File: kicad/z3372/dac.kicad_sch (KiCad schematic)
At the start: 30 parts, among them U13 LM4040AIM3-2.5, U4 TL074, U9 AD5328

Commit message: checkpoint z3372 v0.4
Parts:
- added C27: 10n, Capacitor_SMD:C_0603_1608Metric, symbol Device:C
- added R34: 15k, Resistor_SMD:R_0603_1608Metric, symbol Device:R
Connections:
- net GND: now also C27.2
- net MOD_AMOUNT_VCA3_DAC: no longer U9.13 (VOUT_H)
- net FINAL_VCA4_DAC: now reaches U9.12 (VOUT_G)
- net FINAL_VCA4_DAC: now also R34.1
- new net FINAL_VCA4_CV: C27.1, R34.2
- new net MOD_AMOUNT_DAC: U9.13 (VOUT_H)
- no-connect marks 1 -> 0
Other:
- note added: "AD5328: "B" version works fine. For use at 2X gain output. DAC: 2.5V Reference Voltage B, C, D grades of LM4040 are likely good 'nuff"
- note added: "Pan CVA CV: Take 0V : 5V from DAC shift to -2.5V : 2.5V output 10n cap to give a ~1.6kHz low pass filter TODO: swap inputs and modify filter cap"
- note removed: "AD5328: "B" version works fine. DAC: 2.5V Reference Voltage B, C, D grades of LM4040 are likely good 'nuff"
- note removed: "Pan CVA CV: Take 0V : 5V from DAC shift to -2.5V : 2.5V output 10n cap to give a ~1.6kHz low pass filter"
- title: Z3372 Signal Processing -> Z3372 Signal Processor
- moved on the sheet: C10, C26, C41, C42, C43, C44, C9, R10, R11, R16, R29, R5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

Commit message: schematic done.  some values need tweaking.  design review still needed
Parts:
- removed C10, C27, C44: 10n, Capacitor_SMD:C_0603_1608Metric, symbol Device:C
- removed C39, C7, C8: 0.1u, Capacitor_SMD:C_0603_1608Metric, symbol Device:C
- removed R10, R12, R6, R8: 20k, Resistor_SMD:R_0603_1608Metric, symbol Device:R
- removed R34, R77: 15k, Resistor_SMD:R_0603_1608Metric, symbol Device:R
- removed R47: 4k7, Resistor_SMD:R_1206_3216Metric, symbol Device:R
- removed U13: LM4040AIM3-2.5, Package_TO_SOT_SMD:SOT-23, symbol Reference_Voltage:LM4040DBZ-2.5
- removed U4: TL074, Package_SO:SOIC-14_3.9x8.7mm_P1.27mm, symbol Amplifier_Operational:TL074
- added U3: TL074, Package_SO:SOIC-14_3.9x8.7mm_P1.27mm, symbol Amplifier_Operational:TL074
- C26: value 22n -> 68n; LCSC Part C21122 -> C31658
- U9: symbol as3372_lib:AD5328 -> z3372_lib:AD5328
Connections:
- net FINAL_VCA4_DAC is gone; now on net FINAL_VCA4_CV: U9.12 (VOUT_G)
- net MOD_AMOUNT_VCA3_DAC is gone; now on net MOD_AMOUNT_DAC: R76.1
- net PAN_VCA_CV_DAC is gone; now on net PAN_VCA_CV: U9.5 (VOUT_B)
- net RESONANCE_DAC is gone; now on net RESONANCE_CV: U9.7 (VOUT_D)
- net VREF_2.5V_BUFFERED is gone; now on net VREF_2.5: R7.1
- net VCF_CV: now also U3.8
- net at R11.1, R7.2: now also U3.9 (-)
- net at C9.1, R5.2, R9.2: now also U3.10 (+)
- net MOD_AMOUNT_VCA3_CV renamed MOD_AMOUNT_CV
- net VREF_2.5V renamed VREF_2.5
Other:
- note added: "AS3372 input VCAs: RC lowpass at ~1kHz"
- note added: "Control Voltage level outputs form sheet: Sig1 VCA CV: 0-5V Sig2 VCA CV: 0-5V VCA Mod Level CV: 0-5V Res CV: 0-5V VCF CV: -1 - +6V Pan VCA CV: 0-5V The latter two use opamps to scale; everything else can be straight from DAC. These are slightly outside datasheet specs of 0:5 and -2:+2 to allow for some offset from modulation."
- note added: "Noise lowpass at ~390 Hz, Mod amount at 1 kHz"
- note added: "Sheet totals: Vref impedance: 22k || 22k || 8k2 ==> 4k6"
- note added: "TOOD: adjust RC filters to lower values. Account for 3060VCA range for Noise & Mod TODO: Voltage divider is wrong for 3060"
- note removed: "Control Voltage levels: Sig1 VCA CV: 0-5V Sig2 VCA CV: 0-5V VCA Mod Level CV: 0-5V Res CV: 0-5V VCF CV: -1 - +6V Pan VCA CV: -2.5 - +2.5V The latter two use opamps to scale; everything else can be straight from DAC. These are slightly outside datasheet specs of 0:5 and -2:+2 to allow for some offset from modulation."
- note removed: "Decoupling"
- note removed: "LM4040 resistor rough calc: Ilm4040 min: 70uA Vref input impedance: 10M (buffered)"
- note removed: "Noise Control should be biased to ~0.5V; goes up to 1.67V. RC filter for a lowpass cutoff at ~1200 Hz"
- note removed: "Pan CVA CV: Take 0V : 5V from DAC shift to -2.5V : 2.5V output 10n cap to give a ~1.6kHz low pass filter TODO: swap inputs and modify filter cap"
- note removed: "RC lowpass at ~1kHz"
- note removed: "Res CV has an opamp only to provide a low impedance output for res CV mixing with the res modulation source. If res modulation were to be removed this wouldn't be needed."
- moved on the sheet: C26, C41, C42, C43, C9, R11, R16, R29, R5, R7, R74, R75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

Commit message: review underway for AS3372
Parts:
- removed C9: 68n, Capacitor_SMD:C_0603_1608Metric, symbol Device:C
- removed R11: 3k3, Resistor_SMD:R_0603_1608Metric, symbol Device:R
- removed R7: 8k2, Resistor_SMD:R_0603_1608Metric, symbol Device:R
- removed R9: 120k, Resistor_SMD:R_0603_1608Metric, symbol Device:R
- removed U3: TL074, Package_SO:SOIC-14_3.9x8.7mm_P1.27mm, symbol Amplifier_Operational:TL074
- C26: value 68n -> 0.1u; LCSC Part C31658 -> C14663
- C43: value 10n -> 0.1u; LCSC Part C57112 -> C14663
- R29: value 9k1 -> 11k; LCSC Part C23260 -> (none)
- R5: value 2k4 -> 11k; LCSC Part C22940 -> (none)
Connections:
- net GND: now also R5.1
- net MOD_AMOUNT_CV: now also R5.2
- net VCF_CV: now also U9.4 (VOUT_A)
- removed net VCF_CV_DAC: R5.1, U9.4 (VOUT_A)
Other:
- note added: "Control Voltage level outputs from sheet: VCF CV: 0 -- 5V Pan VCA CV: 0 -- 5V Noise Control Level CV: 0 -- 1.9V Res CV: 0-5V Sig1 VCA CV: 0 -- 5V Sig2 VCA CV: 0 -- 5V Final VCA: 0 -- 5V VCA Mod Level CV: 0 -- 1.9V This sheet _should_ have lowpass filter for all signals. Some signals are filtered off sheet, sorry."
- note added: "DAC lines for 3360 VCA: Voltage divider to 1.9V for linear 3360 input. Cap for lowpass filter of ~230 Hz."
- note removed: "Control Voltage level outputs form sheet: Sig1 VCA CV: 0-5V Sig2 VCA CV: 0-5V VCA Mod Level CV: 0-5V Res CV: 0-5V VCF CV: -1 - +6V Pan VCA CV: 0-5V The latter two use opamps to scale; everything else can be straight from DAC. These are slightly outside datasheet specs of 0:5 and -2:+2 to allow for some offset from modulation."
- note removed: "Noise lowpass at ~390 Hz, Mod amount at 1 kHz"
- note removed: "TOOD: adjust RC filters to lower values. Account for 3060VCA range for Noise & Mod TODO: Voltage divider is wrong for 3060"
- note removed: "VCF Cutoff CV: Take 0V : 5V from DAC shift to -1V : 6V output 68nF cap to give a ~1kHz low pass filter"
- moved on the sheet: C26, C41, C42, C43, R16, R29, R74, R75, R76

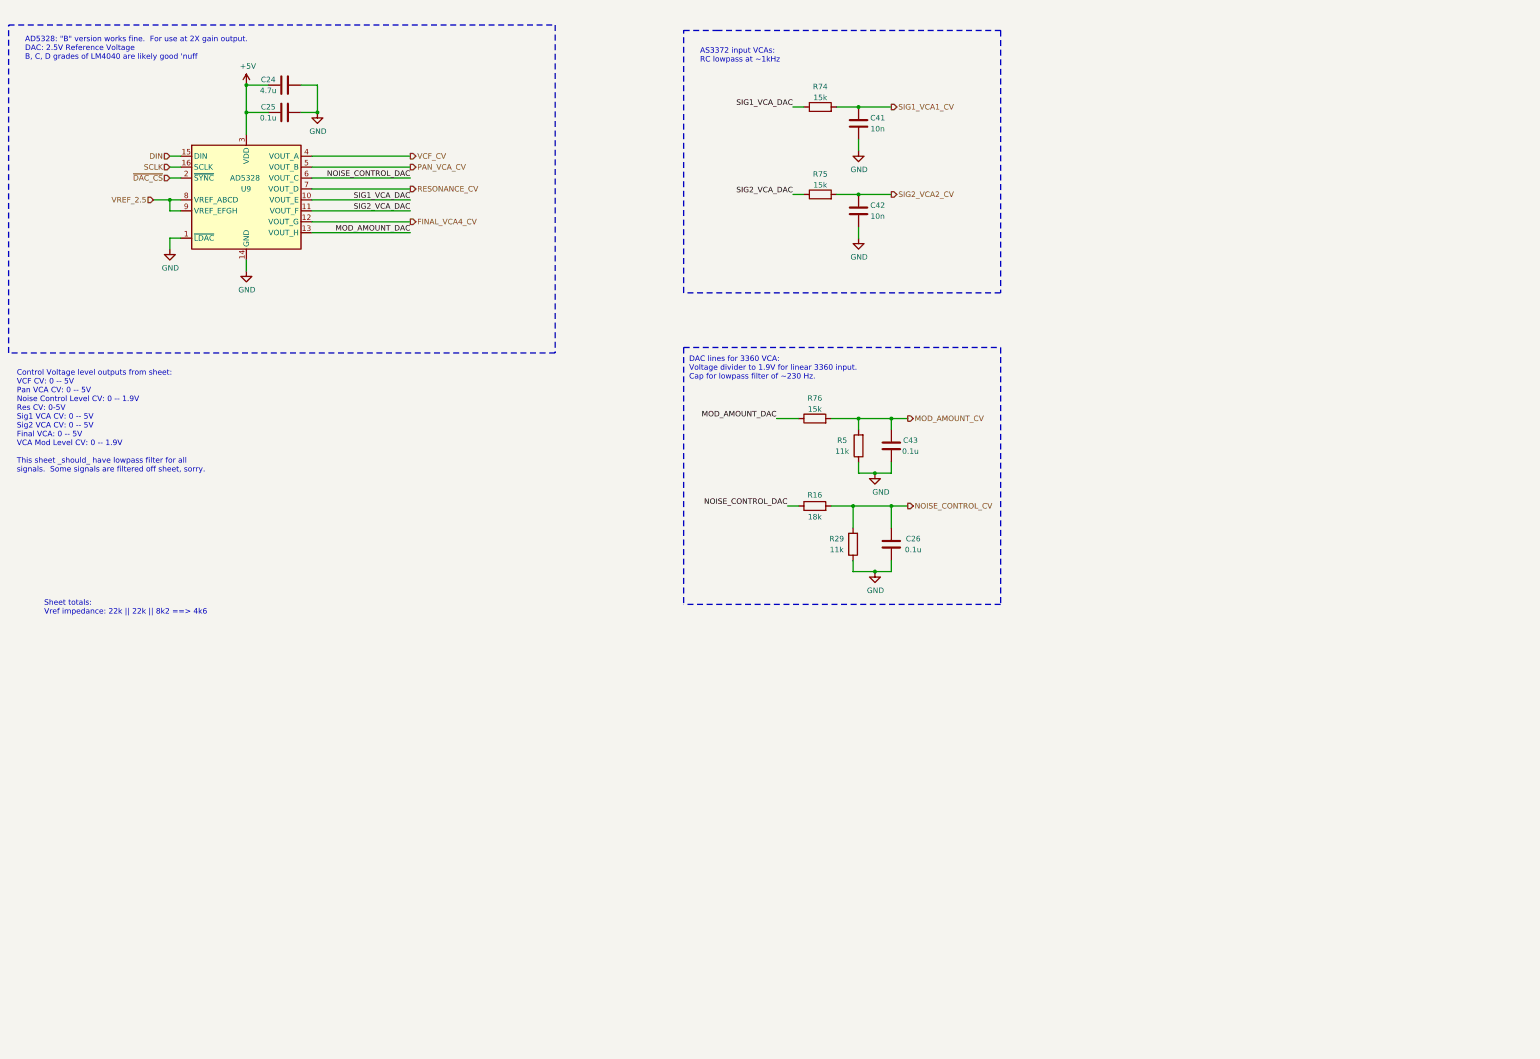
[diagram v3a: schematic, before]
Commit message: schematic completed, working on place and route
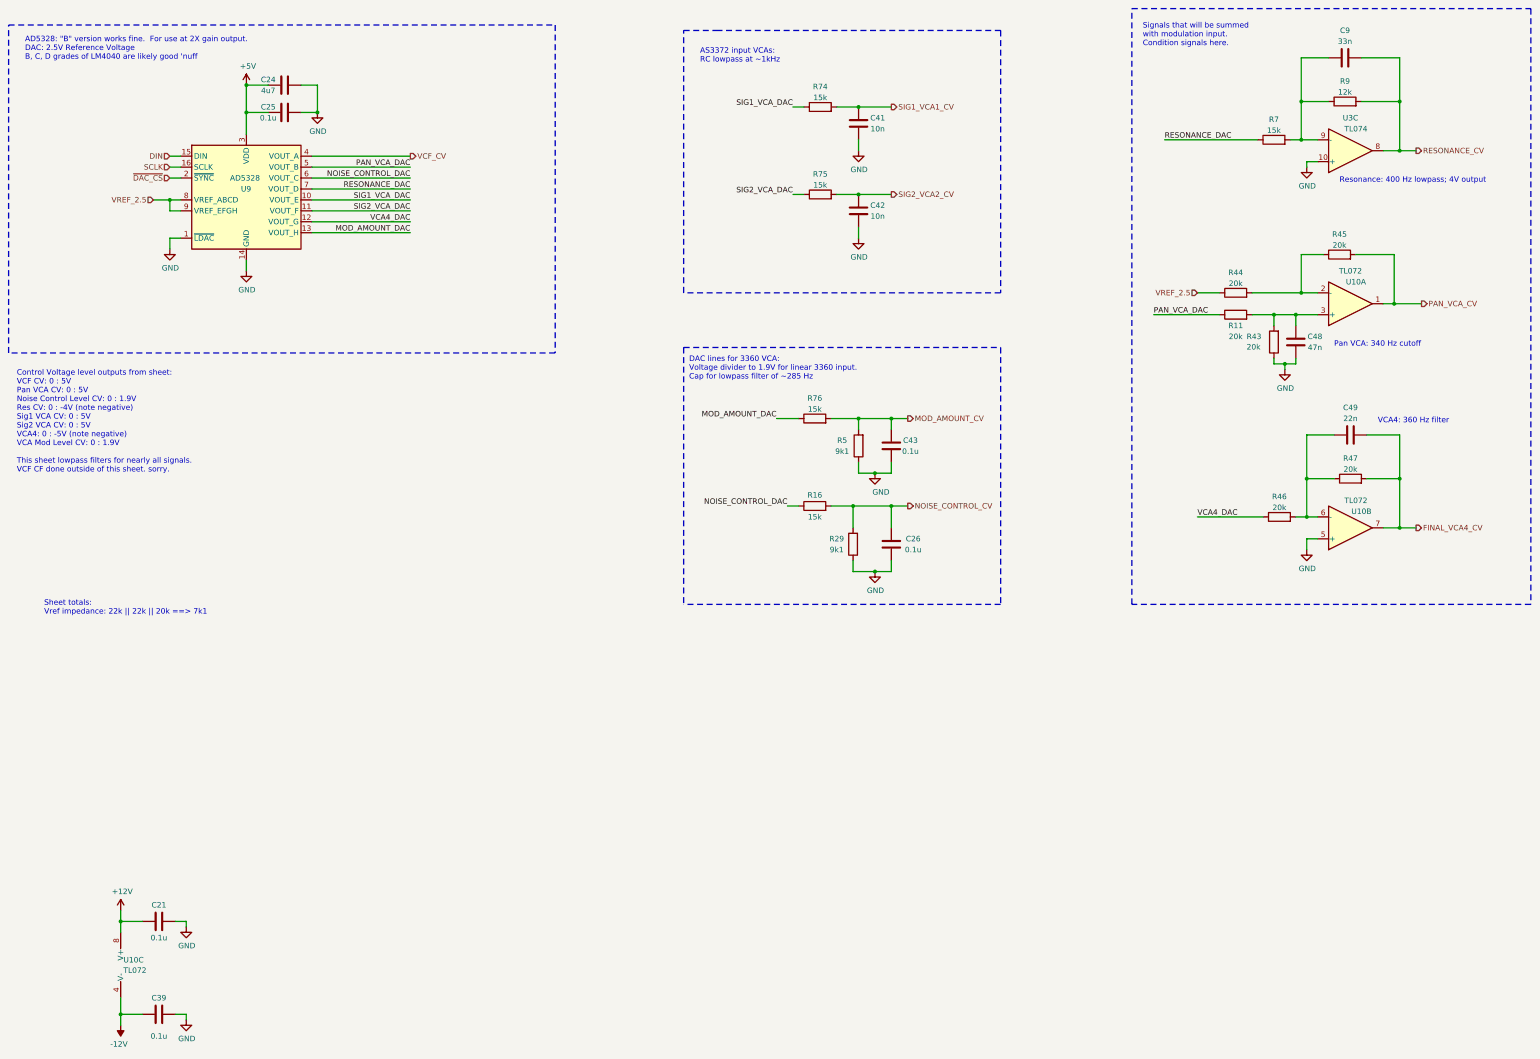
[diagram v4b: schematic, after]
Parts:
- added C21, C39: 0.1u, Capacitor_SMD:C_0603_1608Metric, symbol Device:C
- added C48: 47n, Capacitor_SMD:C_0603_1608Metric, symbol Device:C
- added C49: 22n, Capacitor_SMD:C_0603_1608Metric, symbol Device:C
- added C9: 33n, Capacitor_SMD:C_0603_1608Metric, symbol Device:C
- added R11, R43, R44, R45, R46, R47: 20k, Resistor_SMD:R_0603_1608Metric, symbol Device:R
- added R7: 15k, Resistor_SMD:R_0603_1608Metric, symbol Device:R
- added R9: 12k, Resistor_SMD:R_0603_1608Metric, symbol Device:R
- added U10: TL072, Package_SO:SOIC-8_3.9x4.9mm_P1.27mm, symbol Amplifier_Operational:TL072
- added U3: TL074, Package_SO:TSSOP-14_4.4x5mm_P0.65mm, symbol Amplifier_Operational:TL074
- C24: value 4.7u -> 4u7
- C26: footprint Capacitor_SMD:C_0805_2012Metric -> Capacitor_SMD:C_0603_1608Metric
- R16: value 18k -> 15k; LCSC Part C25810 -> C22809
- R29, R5: value 11k -> 9k1; LCSC Part (none) -> C23260
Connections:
- net FINAL_VCA4_CV: now also C49.2, R47.2, U10.7; no longer U9.12 (VOUT_G)
- net GND: now also C21.2, C39.2, C48.2, R43.1, U10.5 (+), U3.10 (+)
- net PAN_VCA_CV: now also R45.2, U10.1; no longer U9.5 (VOUT_B)
- net RESONANCE_CV: now also C9.2, R9.2, U3.8; no longer U9.7 (VOUT_D)
- net VREF_2.5: now also R44.1
- new net: C9.1, R7.2, R9.1, U3.9 (-)
- new net: C48.1, R11.2, R43.2, U10.3 (+)
- new net: C49.1, R46.2, R47.1, U10.6 (-)
- new net: R44.2, R45.1, U10.2 (-)
- new net +12V: C21.1, U10.8 (V+)
- new net -12V: C39.1, U10.4 (V-)
- new net PAN_VCA_DAC: R11.1, U9.5 (VOUT_B)
- new net RESONANCE_DAC: R7.1, U9.7 (VOUT_D)
- new net VCA4_DAC: R46.1, U9.12 (VOUT_G)
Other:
- note added: "Control Voltage level outputs from sheet: VCF CV: 0 : 5V Pan VCA CV: 0 : 5V Noise Control Level CV: 0 : 1.9V Res CV: 0 : -4V (note negative) Sig1 VCA CV: 0 : 5V Sig2 VCA CV: 0 : 5V VCA4: 0 : -5V (note negative) VCA Mod Level CV: 0 : 1.9V This sheet lowpass filters for nearly all signals. VCF CF done outside of this sheet. sorry."
- note added: "DAC lines for 3360 VCA: Voltage divider to 1.9V for linear 3360 input. Cap for lowpass filter of ~285 Hz"
- note added: "Pan VCA: 340 Hz cutoff"
- note added: "Resonance: 400 Hz lowpass; 4V output"
- note added: "Sheet totals: Vref impedance: 22k || 22k || 20k ==> 7k1"
- note added: "Signals that will be summed with modulation input. Condition signals here."
- note added: "VCA4: 360 Hz filter"
- note removed: "Control Voltage level outputs from sheet: VCF CV: 0 -- 5V Pan VCA CV: 0 -- 5V Noise Control Level CV: 0 -- 1.9V Res CV: 0-5V Sig1 VCA CV: 0 -- 5V Sig2 VCA CV: 0 -- 5V Final VCA: 0 -- 5V VCA Mod Level CV: 0 -- 1.9V This sheet _should_ have lowpass filter for all signals. Some signals are filtered off sheet, sorry."
- note removed: "DAC lines for 3360 VCA: Voltage divider to 1.9V for linear 3360 input. Cap for lowpass filter of ~230 Hz."
- note removed: "Sheet totals: Vref impedance: 22k || 22k || 8k2 ==> 4k6"

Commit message: placement improvements
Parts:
- removed U10: TL072, Package_SO:SOIC-8_3.9x4.9mm_P1.27mm, symbol Amplifier_Operational:TL072
- removed U3: TL074, Package_SO:TSSOP-14_4.4x5mm_P0.65mm, symbol Amplifier_Operational:TL074
- added U12: TL074, Package_SO:TSSOP-14_4.4x5mm_P0.65mm, symbol Amplifier_Operational:TL074
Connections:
- net +12V: now also U12.4 (V+)
- net -12V: now also U12.11 (V-)
- net FINAL_VCA4_CV: now also U12.8
- net GND: now also U12.10 (+), U12.3 (+), U12.5 (+)
- net PAN_VCA_CV: now also U12.14
- net RESONANCE_CV: now also U12.7
- net at C9.1, R7.2, R9.1: now also U12.6 (-)
- net at C48.1, R11.2, R43.2: now also U12.12 (+)
- net at C49.1, R46.2, R47.1: now also U12.9 (-)
- net at R44.2, R45.1: now also U12.13 (-)
- new net: U12.1, U12.2 (-)
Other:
- note added: "Power / Decoupling"
- note added: "Spares"

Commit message: continue routing
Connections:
- net NOISE_CONTROL_DAC: now also U9.4 (VOUT_A); no longer U9.6 (VOUT_C)
- net RESONANCE_DAC: now also U9.6 (VOUT_C); no longer U9.7 (VOUT_D)
- net SIG1_VCA_DAC: now also U9.11 (VOUT_F); no longer U9.10 (VOUT_E)
- net SIG2_VCA_DAC: now also U9.12 (VOUT_G); no longer U9.11 (VOUT_F)
- net VCA4_DAC: now also U9.7 (VOUT_D); no longer U9.12 (VOUT_G)
- net VCF_CV: now also U9.10 (VOUT_E); no longer U9.4 (VOUT_A)
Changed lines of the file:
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@@
     (effects (font (size 1.27 1.27)) (justify left bottom))
   )
-  (label "RESONANCE_DAC" (at 114.3 57.15 180) (fields_autoplaced)
+  (label "RESONANCE_DAC" (at 114.3 54.61 180) (fields_autoplaced)
     (effects (font (size 1.27 1.27)) (justify right bottom))
   )
@@
     (effects (font (size 1.27 1.27)) (justify left bottom))
   )
-  (label "SIG2_VCA_DAC" (at 114.3 62.23 180) (fields_autoplaced)
+  (label "SIG2_VCA_DAC" (at 114.3 64.77 180) (fields_autoplaced)
     (effects (font (size 1.27 1.27)) (justify right bottom))
   )
@@
     (effects (font (size 1.27 1.27)) (justify right bottom))
   )
-  (label "NOISE_CONTROL_DAC" (at 114.3 54.61 180) (fields_autoplaced)
+  (label "NOISE_CONTROL_DAC" (at 114.3 49.53 180) (fields_autoplaced)
     (effects (font (size 1.27 1.27)) (justify right bottom))
   )
@@
     (effects (font (size 1.27 1.27)) (justify right bottom))
   )
-  (label "SIG1_VCA_DAC" (at 114.3 59.69 180) (fields_autoplaced)
+  (label "SIG1_VCA_DAC" (at 114.3 62.23 180) (fields_autoplaced)
     (effects (font (size 1.27 1.27)) (justify right bottom))
   )
@@
     (effects (font (size 1.27 1.27)) (justify right bottom))
   )
-  (label "VCA4_DAC" (at 114.3 64.77 180) (fields_autoplaced)
+  (label "VCA4_DAC" (at 114.3 57.15 180) (fields_autoplaced)
     (effects (font (size 1.27 1.27)) (justify right bottom))
   )
@@
     (effects (font (size 1.27 1.27)) (justify right))
   )
-  (hierarchical_label "VCF_CV" (shape output) (at 114.3 49.53 0) (fields_autoplaced)
+  (hierarchical_label "VCF_CV" (shape output) (at 114.3 59.69 0) (fields_autoplaced)
     (effects (font (size 1.27 1.27)) (justify left))
   )

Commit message: geo reannotate designators
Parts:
- renumbered C26 to C12, C49 to C22, C21 to C24, C48 to C27, C39 to C28, C43 to C4, C25 to C40, C24 to C44, C9 to C7, R7 to R12, R29 to R13, R16 to R29, R46 to R31, R47 to R33, R11 to R34, R9 to R36, R43 to R37, R45 to R40, R44 to R41, R76 to R5, R74 to R51, R75 to R54, R5 to R7, U9 to U12, U12 to U5

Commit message: prep for RTM
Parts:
- C7: value 33n -> 10n; LCSC Part C21117 -> C57112
- R12: value 15k -> 47k; LCSC Part C22809 -> C25819
- R36: value 12k -> 33k; LCSC Part C22790 -> C4216
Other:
- note added: "Control Voltage level outputs from sheet: VCF CV: 0 : 5V Pan VCA CV: 0 : 5V Noise Control Level CV: 0 : 1.9V Res CV: 0 : -3.5V (note negative) Sig1 VCA CV: 0 : 5V Sig2 VCA CV: 0 : 5V VCA4: 0 : -5V (note negative) VCA Mod Level CV: 0 : 1.9V This sheet lowpass filters for nearly all signals. VCF CF done outside of this sheet. sorry."
- note removed: "Control Voltage level outputs from sheet: VCF CV: 0 : 5V Pan VCA CV: 0 : 5V Noise Control Level CV: 0 : 1.9V Res CV: 0 : -4V (note negative) Sig1 VCA CV: 0 : 5V Sig2 VCA CV: 0 : 5V VCA4: 0 : -5V (note negative) VCA Mod Level CV: 0 : 1.9V This sheet lowpass filters for nearly all signals. VCF CF done outside of this sheet. sorry."
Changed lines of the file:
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@@
     (effects (font (size 1.27 1.27)) (justify left bottom))
   )
-  (text "Control Voltage level outputs from sheet:\nVCF CV: 0 : 5V\nPan VCA CV: 0 : 5V\nNoise Control Level CV: 0 : 1.9V\nRes CV: 0 : -4V (note negative)\nSig1 VCA CV: 0 : 5V\nSig2 VCA CV: 0 : 5V\nVCA4: 0 : -5V (note negative)\nVCA Mod Level CV: 0 : 1.9V\n\nThis sheet lowpass filters for nearly all signals.\nVCF CF done outside of this sheet. sorry."
+  (text "Control Voltage level outputs from sheet:\nVCF CV: 0 : 5V\nPan VCA CV: 0 : 5V\nNoise Control Level CV: 0 : 1.9V\nRes CV: 0 : -3.5V (note negative)\nSig1 VCA CV: 0 : 5V\nSig2 VCA CV: 0 : 5V\nVCA4: 0 : -5V (note negative)\nVCA Mod Level CV: 0 : 1.9V\n\nThis sheet lowpass filters for nearly all signals.\nVCF CF done outside of this sheet. sorry."
     (at 22.86 123.19 0)
     (effects (font (size 1.27 1.27)) (justify left bottom))
@@
       (effects (font (size 1.27 1.27)))
     )
-    (property "Value" "15k" (at 314.96 43.5411 90)
+    (property "Value" "47k" (at 314.96 43.5411 90)
       (effects (font (size 1.27 1.27)))
     )
@@
       (effects (font (size 1.27 1.27)) hide)
     )
-    (property "LCSC Part" "C22809" (at 314.96 45.72 0)
+    (property "LCSC Part" "C25819" (at 314.96 45.72 0)
       (effects (font (size 1.27 1.27)) hide)
     )
@@
       (effects (font (size 1.27 1.27)))
     )
-    (property "Value" "12k" (at 331.47 34.6511 90)
+    (property "Value" "33k" (at 331.47 34.6511 90)
       (effects (font (size 1.27 1.27)))
     )
@@
       (effects (font (size 1.27 1.27)) hide)
     )
-    (property "LCSC Part" "C22790" (at 331.47 36.83 0)
+    (property "LCSC Part" "C4216" (at 331.47 36.83 0)
       (effects (font (size 1.27 1.27)) hide)
     )
@@
       (effects (font (size 1.27 1.27)))
     )
-    (property "Value" "33n" (at 331.47 22.86 90)
+    (property "Value" "10n" (at 331.47 22.86 90)
       (effects (font (size 1.27 1.27)))
     )
@@
       (effects (font (size 1.27 1.27)) hide)
     )
-    (property "LCSC Part" "C21117" (at 331.47 26.67 0)
-      (effects (font (size 1.27 1.27)) hide)
-    )
+    (property "LCSC Part" "C57112" (at 331.47 26.67 0)
+      (effects (font (size 1.27 1.27)) hide)
+    )
